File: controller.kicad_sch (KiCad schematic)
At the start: 27 parts, among them J1 Conn_ST_STDC14, P1 USB_C_Plug_USB2.0, SW1 SW_Push, SW2 SW_Push, U1 STM32L476RGTx, U2 BD33FC0FP, U3 NUP2202

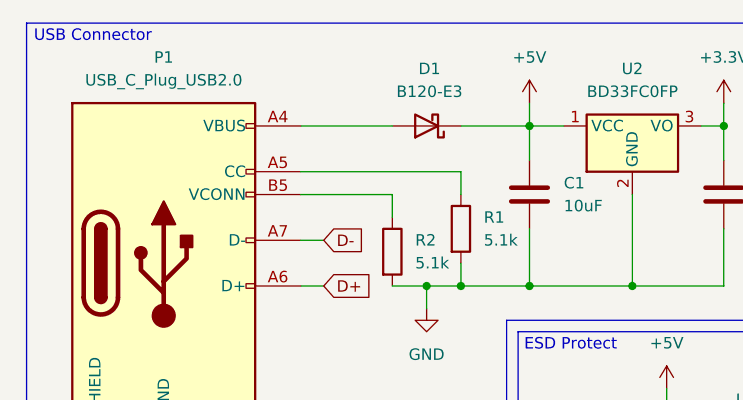
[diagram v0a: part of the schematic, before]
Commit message: initial ground/power routing
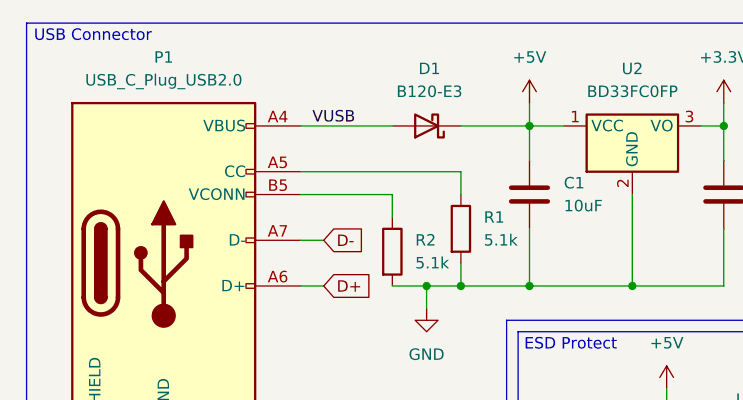
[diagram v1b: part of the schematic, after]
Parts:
- P1: footprint Connector_USB:USB_C_Plug_Molex_105444 -> Connector_USB:USB_C_Receptacle_GCT_USB4085
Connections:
- net VUSB: now reaches D1.2 (A), P1.A4 (VBUS), P1.A9 (VBUS), P1.B4 (VBUS), P1.B9 (VBUS)
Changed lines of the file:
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@@
 	(wire
 		(pts
-			(xy 43.18 24.13) (xy 53.34 24.13)
-		)
-		(stroke
-			(width 0)
-			(type default)
-		)
-	)
-	(wire
-		(pts
 			(xy 44.45 99.06) (xy 44.45 101.6)
 		)
@@
 	(wire
 		(pts
+			(xy 43.18 24.13) (xy 53.34 24.13)
+		)
+		(stroke
+			(width 0)
+			(type default)
+		)
+	)
+	(wire
+		(pts
 			(xy 153.67 63.5) (xy 152.4 63.5)
 		)
@@
 		)
 	)
+	(label "VUSB"
+		(at 44.45 24.13 0)
+		(fields_autoplaced yes)
+		(effects
+			(font
+				(size 1.27 1.27)
+			)
+			(justify left bottom)
+		)
+		(property "Netclass" "Power"
+			(at 44.45 25.4 0)
+			(effects
+				(font
+					(size 1.27 1.27)
+					(italic yes)
+				)
+				(justify left)
+			)
+		)
+	)
 	(global_label "SWDIO"
 		(shape input)
@@
 			)
 		)
-		(property "Footprint" "Connector_USB:USB_C_Plug_Molex_105444"
+		(property "Footprint" "Connector_USB:USB_C_Receptacle_GCT_USB4085"
 			(at 31.75 39.37 0)
 			(effects

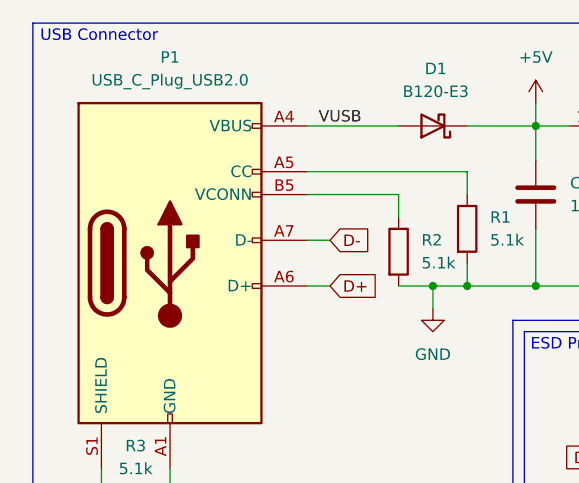
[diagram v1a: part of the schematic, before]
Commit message: change to receptacle
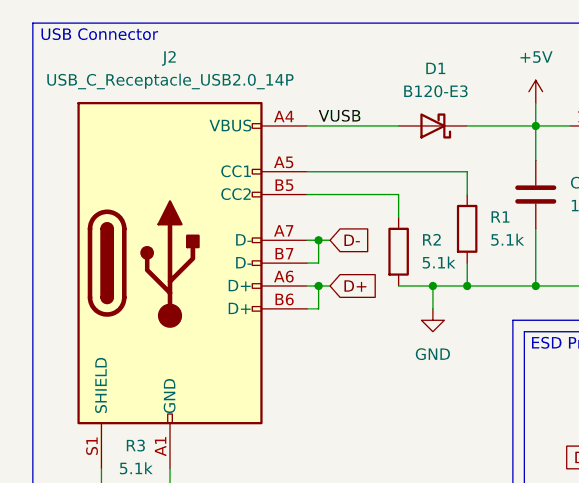
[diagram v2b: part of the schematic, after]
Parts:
- removed P1: USB_C_Plug_USB2.0, Connector_USB:USB_C_Receptacle_GCT_USB4085, symbol Connector:USB_C_Plug_USB2.0
- added J2: USB_C_Receptacle_USB2.0_14P, symbol Connector:USB_C_Receptacle_USB2.0_14P
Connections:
- net D+: now also J2.A6 (D+), J2.B6 (D+)
- net D-: now also J2.A7 (D-), J2.B7 (D-)
- net GND: now also J2.A1 (GND), J2.A12 (GND), J2.B1 (GND), J2.B12 (GND)
- net VUSB: now also J2.A4 (VBUS), J2.A9 (VBUS), J2.B4 (VBUS), J2.B9 (VBUS)
- net at R1.1: now also J2.A5 (CC1)
- net at R2.1: now also J2.B5 (CC2)
- net at R3.1: now also J2.S1 (SHIELD)
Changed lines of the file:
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@@
 	)
 	(junction
+		(at 44.45 36.83)
+		(diameter 0)
+		(color 0 0 0 0)
+	)
+	(junction
 		(at 16.51 88.9)
 		(diameter 0)
@@
 	)
 	(junction
+		(at 44.45 41.91)
+		(diameter 0)
+		(color 0 0 0 0)
+	)
+	(junction
 		(at 77.47 88.9)
 		(diameter 0)
@@
 	(wire
 		(pts
+			(xy 44.45 36.83) (xy 45.72 36.83)
+		)
+		(stroke
+			(width 0)
+			(type default)
+		)
+	)
+	(wire
+		(pts
 			(xy 16.51 88.9) (xy 16.51 91.44)
 		)
@@
 	(wire
 		(pts
+			(xy 44.45 39.37) (xy 44.45 36.83)
+		)
+		(stroke
+			(width 0)
+			(type default)
+		)
+	)
+	(wire
+		(pts
 			(xy 62.23 121.92) (xy 59.69 121.92)
 		)
@@
 	(wire
 		(pts
+			(xy 44.45 44.45) (xy 44.45 41.91)
+		)
+		(stroke
+			(width 0)
+			(type default)
+		)
+	)
+	(wire
+		(pts
+			(xy 43.18 44.45) (xy 44.45 44.45)
+		)
+		(stroke
+			(width 0)
+			(type default)
+		)
+	)
+	(wire
+		(pts
 			(xy 44.45 99.06) (xy 44.45 101.6)
 		)
@@
 	(wire
 		(pts
-			(xy 43.18 36.83) (xy 45.72 36.83)
+			(xy 43.18 36.83) (xy 44.45 36.83)
 		)
 		(stroke
@@
 	(wire
 		(pts
+			(xy 43.18 39.37) (xy 44.45 39.37)
+		)
+		(stroke
+			(width 0)
+			(type default)
+		)
+	)
+	(wire
+		(pts
 			(xy 119.38 29.21) (xy 125.73 29.21)
 		)
@@
 	(wire
 		(pts
-			(xy 43.18 41.91) (xy 45.72 41.91)
+			(xy 43.18 41.91) (xy 44.45 41.91)
 		)
 		(stroke
@@
 	(wire
 		(pts
+			(xy 44.45 41.91) (xy 45.72 41.91)
+		)
+		(stroke
+			(width 0)
+			(type default)
+		)
+	)
+	(wire
+		(pts
 			(xy 44.45 88.9) (xy 44.45 91.44)
 		)
@@
 	)
 	(symbol
+		(lib_id "Connector:USB_C_Receptacle_USB2.0_14P")
+		(at 27.94 39.37 0)
+		(unit 1)
+		(exclude_from_sim no)
+		(in_bom yes)
+		(on_board yes)
+		(dnp no)
+		(fields_autoplaced yes)
+		(property "Reference" "J2"
+			(at 27.94 16.51 0)
+			(effects
+				(font
+					(size 1.27 1.27)
+				)
+			)
+		)
+		(property "Value" "USB_C_Receptacle_USB2.0_14P"
+			(at 27.94 19.05 0)
+			(effects
+				(font
+					(size 1.27 1.27)
+				)
+			)
+		)
+		(property "Footprint" ""
+			(at 31.75 39.37 0)
+			(effects
+				(font
+					(size 1.27 1.27)
+				)
+				(hide yes)
+			)
+		)
+		(property "Datasheet" "https://www.usb.org/sites/default/files/documents/usb_type-c.zip"
+			(at 31.75 39.37 0)
+			(effects
+				(font
+					(size 1.27 1.27)
+				)
+				(hide yes)
+			)
+		)
+		(property "Description" "USB 2.0-only 14P Type-C Receptacle connector"
+			(at 27.94 39.37 0)
+			(effects
+				(font
+					(size 1.27 1.27)
+				)
+				(hide yes)
+			)
+		)
+		(pin "A7"
+		)
+		(pin "B4"
+		)
+		(pin "B5"
+		)
+		(pin "B7"
+		)
+		(pin "B9"
+		)
+		(pin "A5"
+		)
+		(pin "B6"
+		)
+		(pin "A9"
+		)
+		(pin "A1"
+		)
+		(pin "A6"
+		)
+		(pin "S1"
+		)
+		(pin "A12"
+		)
+		(pin "A4"
+		)
+		(pin "B12"
+		)
+		(pin "B1"
+		)
+		(instances
+			(project ""
+				(path "/8767df91-471e-42dd-a6da-5f13f49512a3"
+					(reference "J2")
+					(unit 1)
+				)
+			)
+		)
+	)
+	(symbol
 		(lib_id "Device:C")
 		(at 30.48 93.98 90)
@@
 					(unit 1)
 				)
-			)
-		)
-	)
-	(symbol
-		(lib_id "Connector:USB_C_Plug_USB2.0")
-		(at 27.94 39.37 0)
-		(unit 1)
-		(exclude_from_sim no)
-		(in_bom yes)
-		(on_board yes)
-		(dnp no)
-		(fields_autoplaced yes)
-		(property "Reference" "P1"
-			(at 27.94 16.51 0)
-			(effects
-				(font
-					(size 1.27 1.27)
-				)
-			)
-		)
-		(property "Value" "USB_C_Plug_USB2.0"
-			(at 27.94 19.05 0)
-			(effects
-				(font
-					(size 1.27 1.27)
-				)
-			)
-		)
-		(property "Footprint" "Connector_USB:USB_C_Receptacle_GCT_USB4085"
-			(at 31.75 39.37 0)
-			(effects
-				(font
-					(size 1.27 1.27)
-				)
-				(hide yes)
-			)
-		)
-		(property "Datasheet" "https://www.usb.org/sites/default/files/documents/usb_type-c.zip"
-			(at 31.75 39.37 0)
-			(effects
-				(font
-					(size 1.27 1.27)
-				)
-				(hide yes)
-			)
-		)
-		(property "Description" "USB 2.0-only Type-C Plug connector"
-			(at 27.94 39.37 0)
-			(effects
-				(font
-					(size 1.27 1.27)
-				)
-				(hide yes)
-			)
-		)
-		(pin "B9"
-		)
-		(pin "A5"
-		)
-		(pin "A7"
-		)
-		(pin "B5"
-		)
-		(pin "A6"
-		)
-		(pin "B4"
-		)
-		(pin "A9"
-		)
-		(pin "A4"
-		)
-		(pin "B12"
-		)
-		(pin "B1"
-		)
-		(pin "A12"
-		)
-		(pin "S1"
-		)
-		(pin "A1"
-		)
-		(instances
-			(project "controller"
-				(path "/8767df91-471e-42dd-a6da-5f13f49512a3"
-					(reference "P1")
-					(unit 1)
-				)

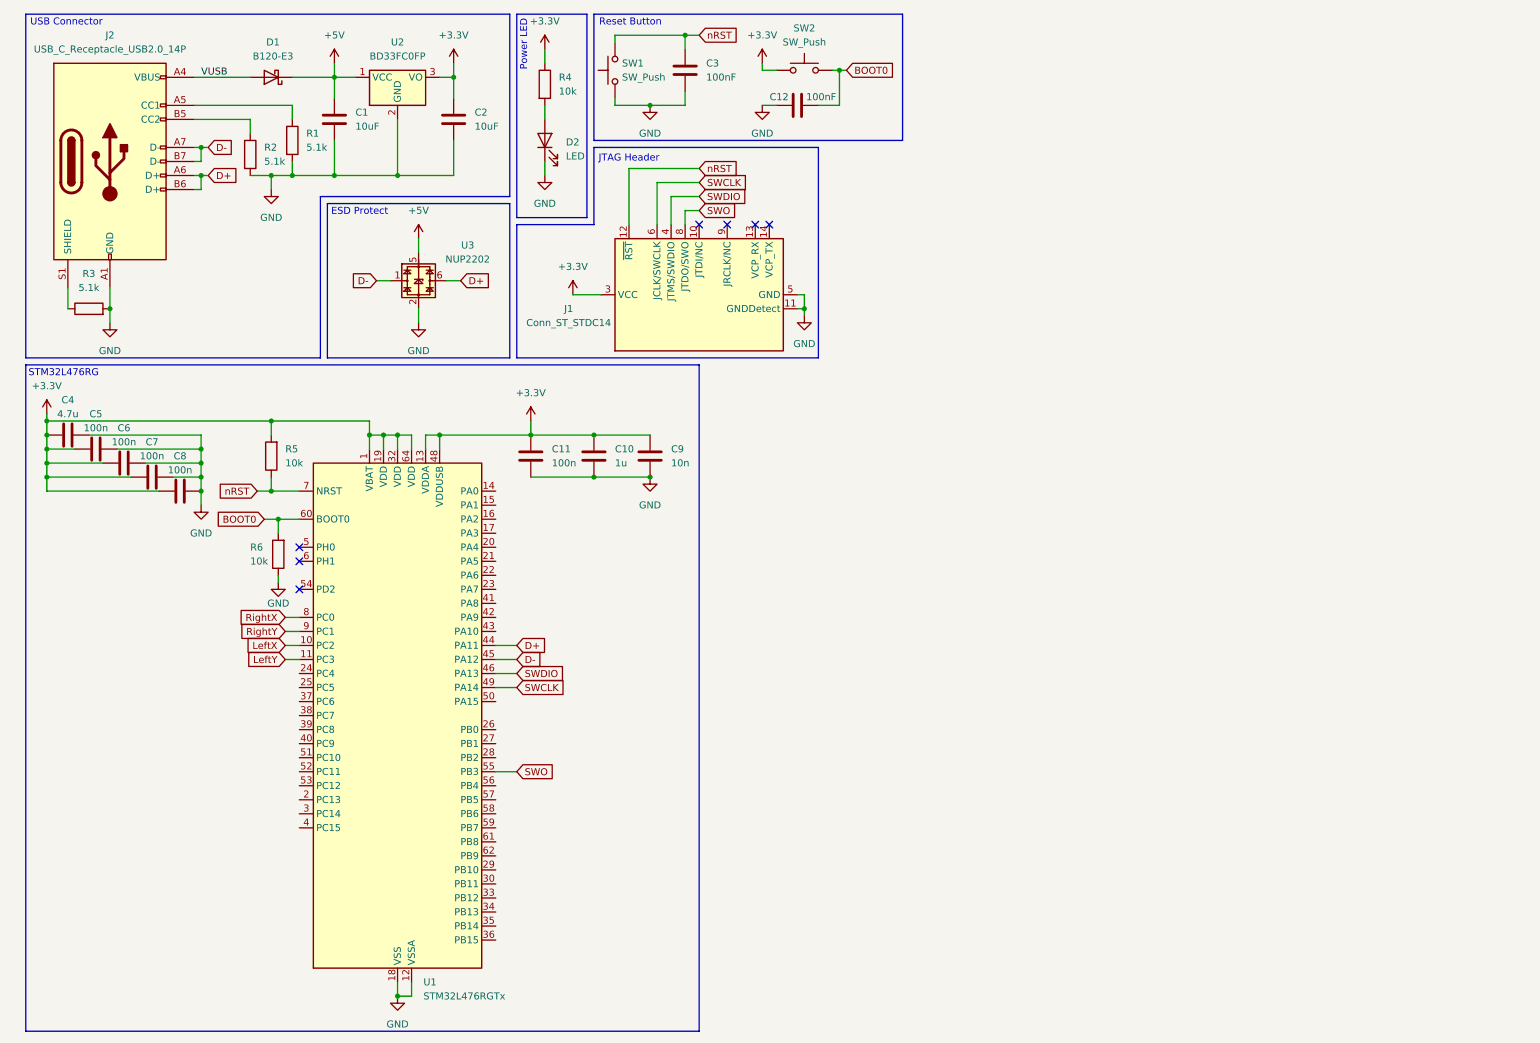
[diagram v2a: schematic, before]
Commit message: add some control components to schematic and pcb
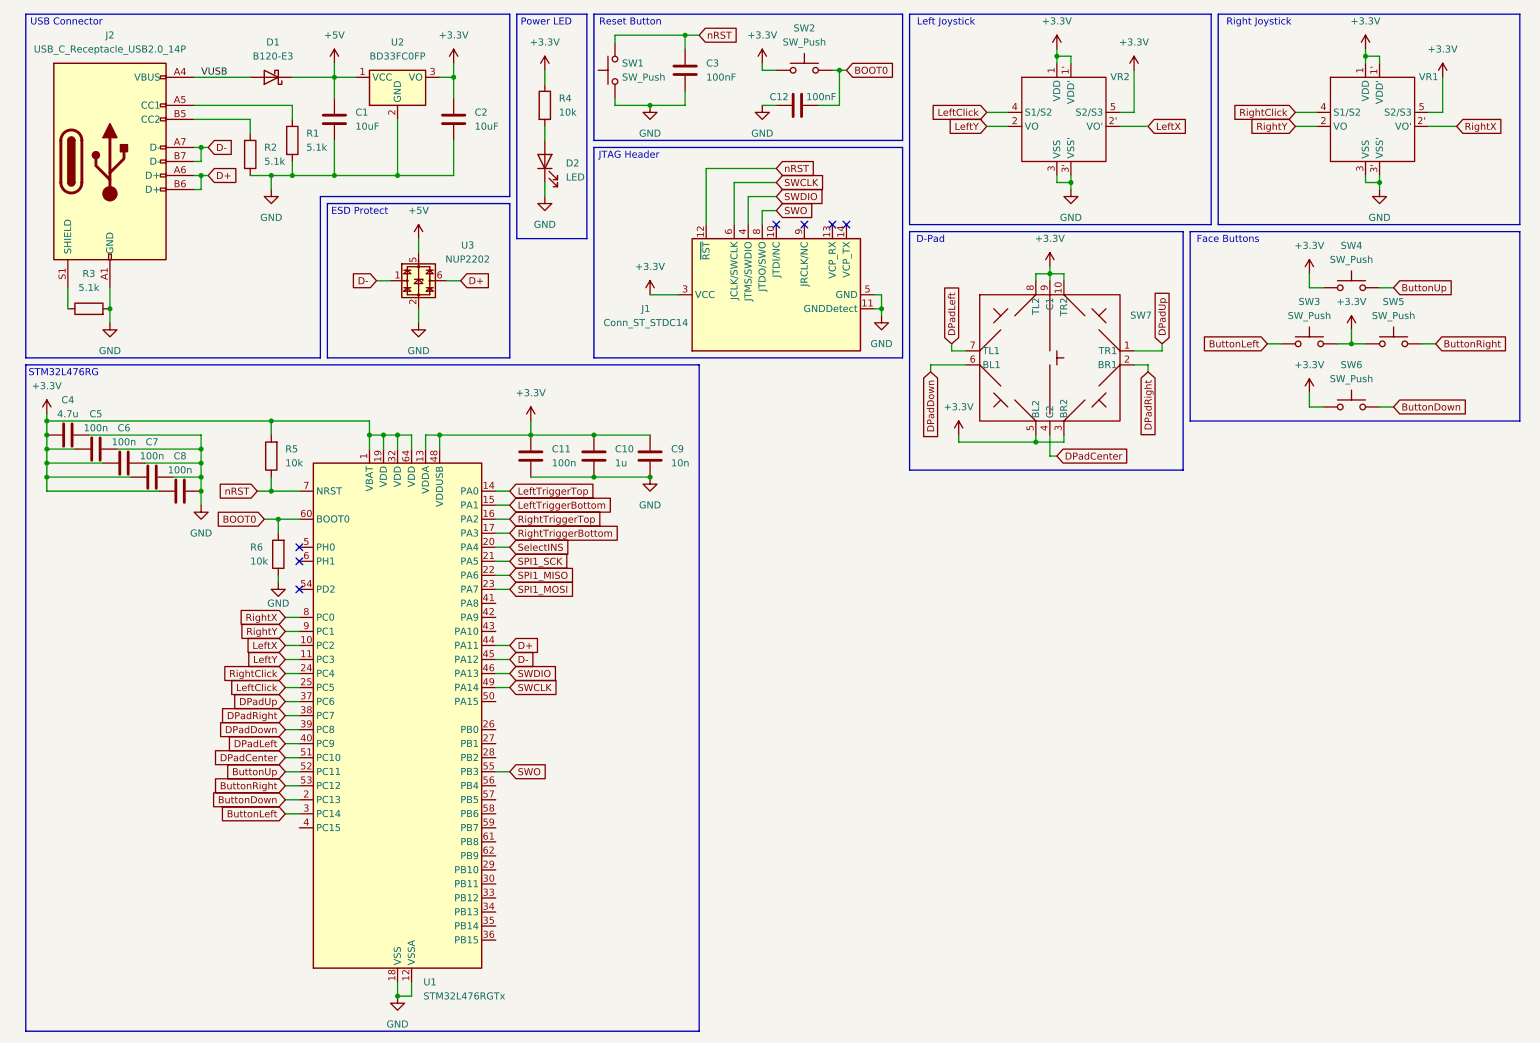
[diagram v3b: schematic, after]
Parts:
- added SW3, SW4, SW5, SW6: SW_Push, symbol Switch:SW_Push
- added SW7: ~, K1-1210UN-01:K1-1210UN-01, symbol K1-1210UN-01:K1-1210UN-01
- added VR1, VR2: ~, 3D16A1N:3D16A1N, symbol 3D16:3D16A1N-T-50
- J2: footprint (none) -> Connector_USB:USB_C_Receptacle_GCT_USB4085
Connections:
- net +3.3V: now also SW3.2, SW4.1, SW5.1, SW6.1, SW7.10 (TR2), SW7.3 (BR2), SW7.5 (BL2), SW7.8 (TL2), SW7.9 (C1), VR1.1 (VDD), VR1.1' (VDD'), VR1.5 (S2/S3), VR2.1 (VDD), VR2.1' (VDD'), VR2.5 (S2/S3)
- net GND: now also VR1.3 (VSS), VR1.3' (VSS'), VR2.3 (VSS), VR2.3' (VSS')
- net LeftX: now also VR2.2' (VO')
- net LeftY: now also VR2.2 (VO)
- net RightX: now also VR1.2' (VO')
- net RightY: now also VR1.2 (VO)
- net LeftTriggerTop: now reaches U1.14 (PA0)
- net LeftTriggerBottom: now reaches U1.15 (PA1)
- net RightTriggerTop: now reaches U1.16 (PA2)
- net RightTriggerBottom: now reaches U1.17 (PA3)
- net ButtonDown: now reaches U1.2 (PC13)
- net ButtonDown: now also SW6.2
- net SelectINS: now reaches U1.20 (PA4)
- net SPI1_SCK: now reaches U1.21 (PA5)
- net SPI1_MISO: now reaches U1.22 (PA6)
- net SPI1_MOSI: now reaches U1.23 (PA7)
- net RightClick: now reaches U1.24 (PC4)
- net RightClick: now also VR1.4 (S1/S2)
- net LeftClick: now reaches U1.25 (PC5)
- net LeftClick: now also VR2.4 (S1/S2)
- net ButtonLeft: now reaches U1.3 (PC14)
- net ButtonLeft: now also SW3.1
- net DPadUp: now reaches U1.37 (PC6)
- net DPadUp: now also SW7.1 (TR1)
- net DPadRight: now reaches U1.38 (PC7)
- net DPadRight: now also SW7.2 (BR1)
- net DPadDown: now reaches U1.39 (PC8)
- net DPadDown: now also SW7.6 (BL1)
- net DPadLeft: now reaches U1.40 (PC9)
- net DPadLeft: now also SW7.7 (TL1)
- net DPadCenter: now reaches U1.51 (PC10)
- net DPadCenter: now also SW7.4 (C2)
- net ButtonUp: now reaches U1.52 (PC11)
- net ButtonUp: now also SW4.2
- net ButtonRight: now reaches U1.53 (PC12)
- net ButtonRight: now also SW5.2
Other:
- note added: "D-Pad"
- note added: "Face Buttons"
- note added: "Left Joystick"
- note added: "Right Joystick"
- moved on the sheet: D2, J1, R4

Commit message: finish routing, more or less
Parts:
- added R10, R11, R12, R13, R14, R7, R8, R9: 10k, Resistor_SMD:R_0201_0603Metric, symbol Device:R
- added SW10, SW11, SW8, SW9: SW_Push, Button_Switch_SMD:SW_Push_1P1T-MP_NO_Horizontal_Alps_SKRTLAE010, symbol Switch:SW_Push
- SW3, SW4, SW5, SW6: footprint (none) -> Button_Switch_SMD:SW_Push_1P1T_NO_CK_PTS125Sx43SMTR
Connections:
- net +3.3V: now also SW10.1, SW11.1, SW8.1, SW9.1
- net ButtonDown: now also R10.1
- net ButtonLeft: now also R7.1
- net ButtonRight: now also R8.1
- net ButtonUp: now also R9.2
- net GND: now also R10.2, R11.2, R12.2, R13.2, R14.2, R7.2, R8.2, R9.1
- net LeftTriggerBottom: now also R12.1, SW9.2
- net LeftTriggerTop: now also R11.1, SW8.2
- net LeftX: now also U1.8 (PC0); no longer U1.10 (PC2)
- net LeftY: now also U1.9 (PC1); no longer U1.11 (PC3)
- net RightTriggerBottom: now also R14.1, SW11.2
- net RightTriggerTop: now also R13.1, SW10.2
- net RightX: now also U1.10 (PC2); no longer U1.8 (PC0)
- net RightY: now also U1.11 (PC3); no longer U1.9 (PC1)
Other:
- moved on the sheet: SW3, SW5, SW6
